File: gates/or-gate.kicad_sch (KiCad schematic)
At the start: 5 parts

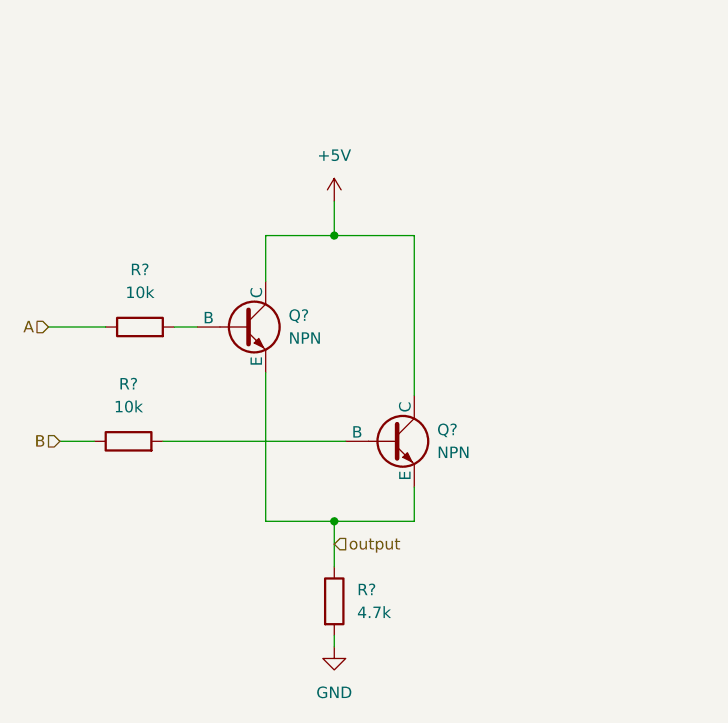
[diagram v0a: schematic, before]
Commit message: replaced circuitry in half adder with reusable gates
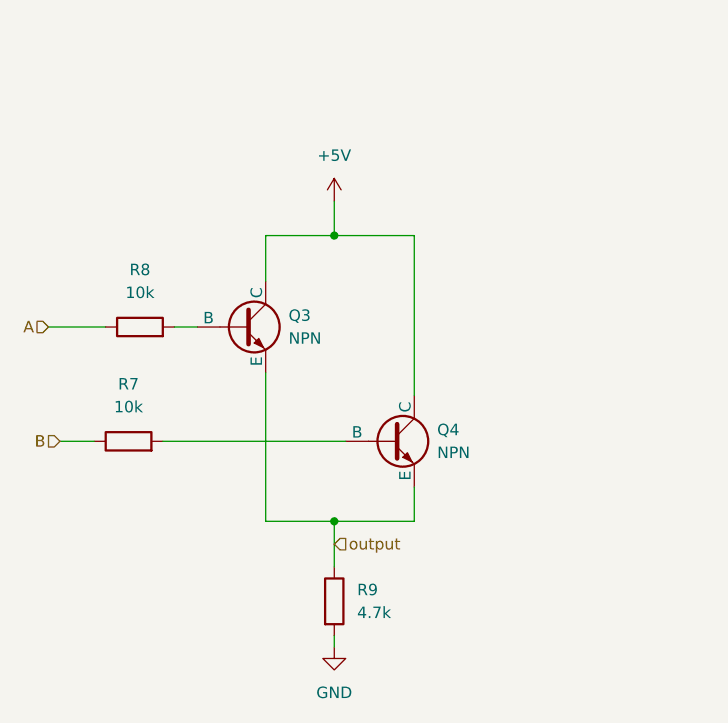
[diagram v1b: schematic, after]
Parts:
- removed Q? (x2): NPN, symbol Simulation_SPICE:NPN
- removed R?: 4.7k, symbol Device:R
- removed R? (x2): 10k, symbol Device:R
- added Q3, Q4: NPN, symbol Simulation_SPICE:NPN
- added R7, R8: 10k, symbol Device:R
- added R9: 4.7k, symbol Device:R
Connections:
- net +5V: now also Q3.1 (C), Q4.1 (C)
- net A: now also R8.1
- net B: now also R7.1
- net GND: now also R9.2
- net output: now also Q3.3 (E), Q4.3 (E), R9.1
- new net: Q4.2 (B), R7.2
- new net: Q3.2 (B), R8.2

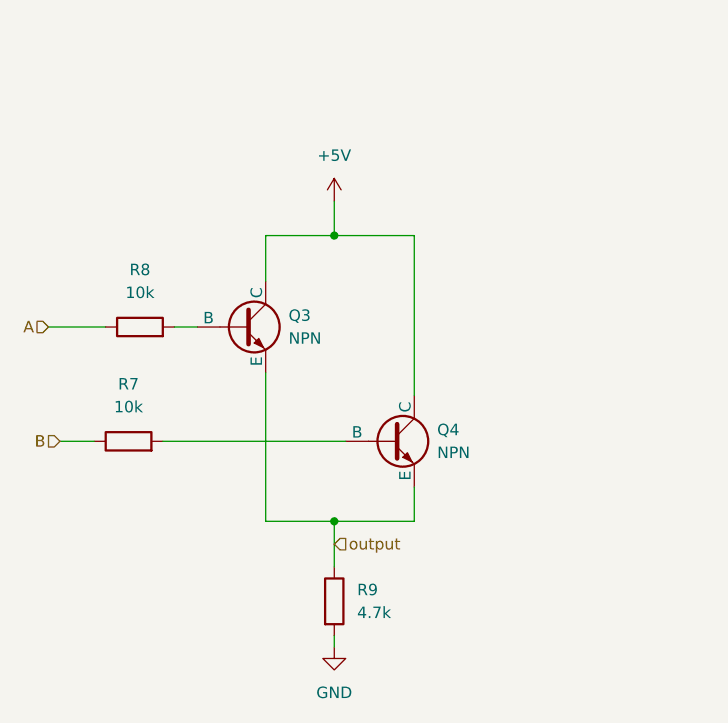
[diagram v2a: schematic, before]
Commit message: Fixed gates and moved half adder to its own directory
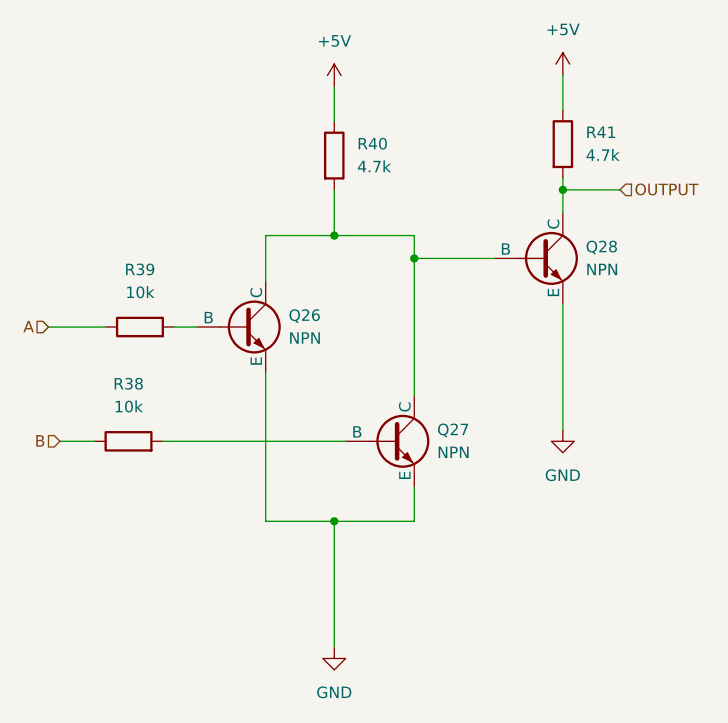
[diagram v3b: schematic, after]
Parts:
- removed R9: 4.7k, symbol Device:R
- added Q28: NPN, symbol Simulation_SPICE:NPN
- added R40, R41: 4.7k, symbol Device:R
- renumbered Q3 to Q26, Q4 to Q27, R7 to R38, R8 to R39
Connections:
- net output is gone; now on net GND: Q26.3 (E), Q27.3 (E)
- net +5V: now also R40.1, R41.1; no longer Q26.1 (C), Q27.1 (C)
- net GND: now also Q28.3 (E)
- new net: Q26.1 (C), Q27.1 (C), Q28.2 (B), R40.2
- new net OUTPUT: Q28.1 (C), R41.2
